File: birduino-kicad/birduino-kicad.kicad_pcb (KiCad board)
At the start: 2 copper layers, 47.5 x 71.9 mm, 38 parts, among them J1 Conn_01x03_Male, J10 Conn_01x02_Male, J11 Conn_01x01_Male, J2 Conn_01x02_Male, J3 Conn_02x05_Odd_Even, J4 Conn_01x04, J5 Conn_01x01_Male, J6 Conn_01x01_Male, J7 Conn_01x01_Male, J8 Conn_02x02_Odd_Even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

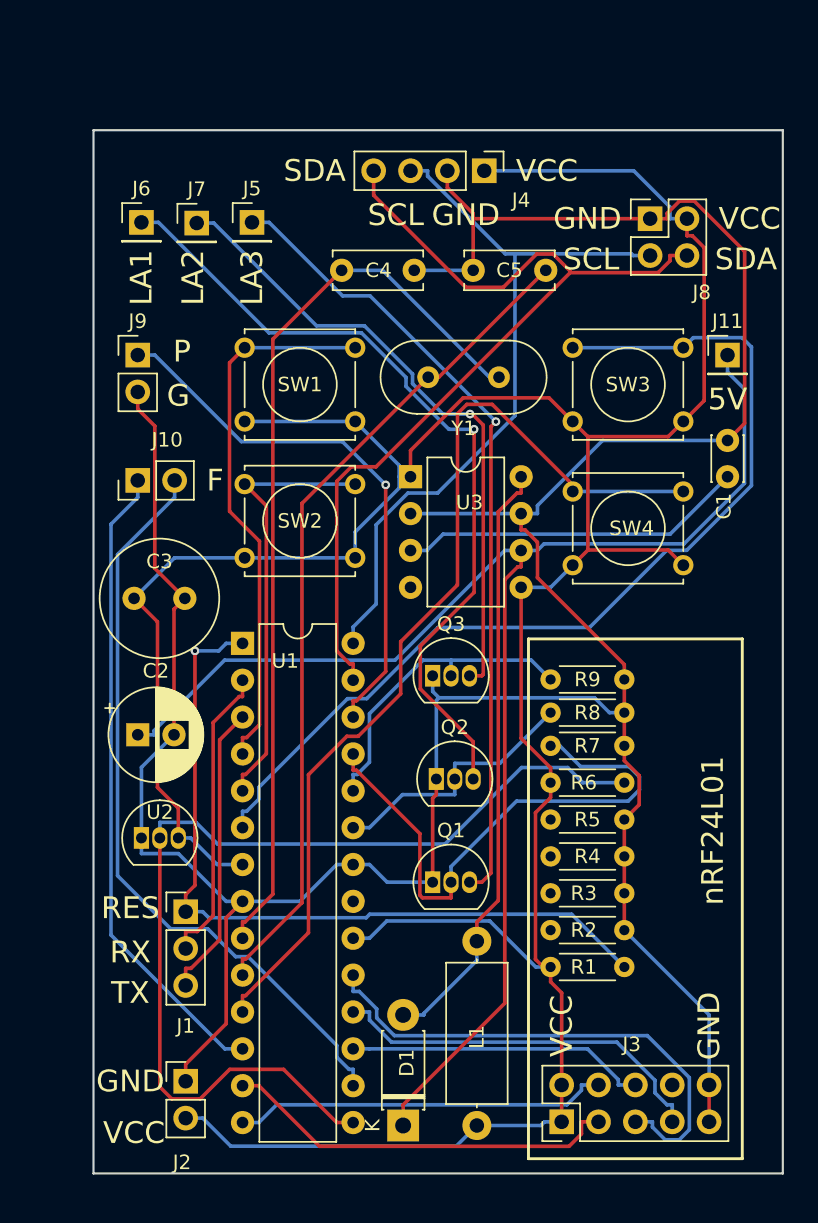
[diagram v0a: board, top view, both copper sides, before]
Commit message: feat: add fixation holes. First fabrication files. Version 1.0 closed for production.
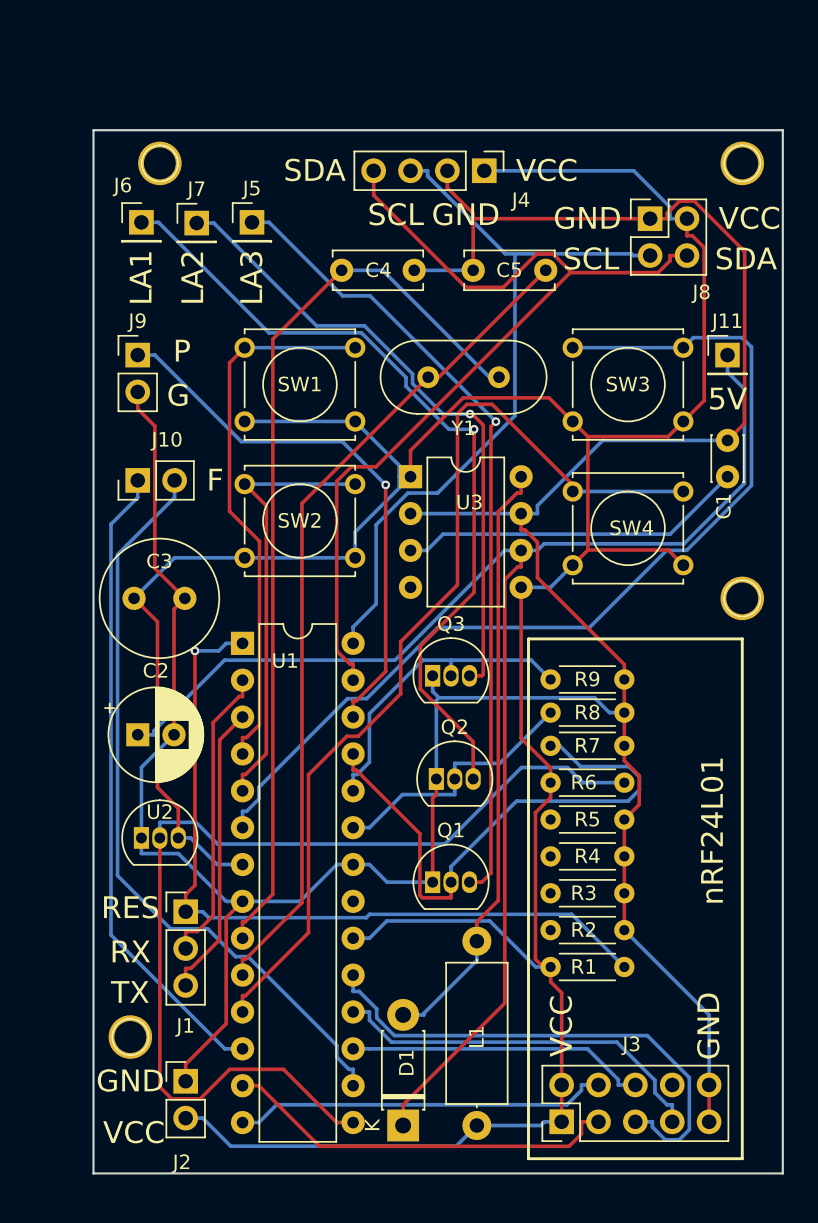
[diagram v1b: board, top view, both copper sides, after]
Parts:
- added ?: Pin_D1.0mm_L10.0mm, Connector_Pin:Pin_D1.0mm_L10.0mm, F.Cu at (133.3, 81.5)
- added ?: Pin_D1.0mm_L10.0mm, Connector_Pin:Pin_D1.0mm_L10.0mm, F.Cu at (173.5, 111.5)
- added ?: Pin_D1.0mm_L10.0mm, Connector_Pin:Pin_D1.0mm_L10.0mm, F.Cu at (173.5, 81.5)
- added ?: Pin_D1.0mm_L10.0mm, Connector_Pin:Pin_D1.0mm_L10.0mm, F.Cu at (131.3, 141.7)
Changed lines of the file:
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@@
     (tracks 429)
     (zones 0)
-    (modules 38)
+    (modules 42)
     (nets 32)
   )
@@
     (mod_text_size 1 1)
     (mod_text_width 0.15)
-    (pad_size 1.524 1.524)
-    (pad_drill 0.762)
+    (pad_size 3 3)
+    (pad_drill 2.2)
     (pad_to_mask_clearance 0.2)
     (solder_mask_min_width 0.25)
@@
     (visible_elements FFFFFF7F)
     (pcbplotparams
-      (layerselection 0x00030_80000001)
+      (layerselection 0x00030_ffffffff)
       (usegerberextensions false)
       (usegerberattributes false)
@@
       (outputformat 1)
       (mirror false)
-      (drillshape 1)
+      (drillshape 0)
       (scaleselection 1)
-      (outputdirectory ""))
+      (outputdirectory "../fabrication"))
   )
   (net 0 "")
@@
     (add_net XTAL2)
   )
+  (module Connector_Pin:Pin_D1.0mm_L10.0mm (layer F.Cu)
+    (at 133.35 81.534)
+    (descr "solder Pin_ diameter 1.0mm, hole diameter 1.0mm (press fit), length 10.0mm")
+    (tags "solder Pin_ press fit")
+    (fp_text reference "" (at -4.064 -0.508) (layer F.SilkS) hide
+      (effects (font (size 1 1) (thickness 0.15)))
+    )
+    (fp_text value Pin_D1.0mm_L10.0mm (at 0 -2.05) (layer F.Fab)
+      (effects (font (size 1 1) (thickness 0.15)))
+    )
+    (fp_text user %R (at 0 2.25) (layer F.Fab)
+      (effects (font (size 1 1) (thickness 0.15)))
+    )
+    (fp_circle (center 0 0) (end 1.5 0) (layer F.CrtYd) (width 0.05))
+    (fp_circle (center 0 0) (end 0.5 0) (layer F.Fab) (width 0.12))
+    (fp_circle (center 0 0) (end 1 0) (layer F.Fab) (width 0.12))
+    (fp_circle (center 0 0) (end 1.25 0.05) (layer F.SilkS) (width 0.12))
+    (pad 1 thru_hole circle (at 0 0) (size 3 3) (drill 2.2) (layers *.Cu *.Mask))
+    (model ${KISYS3DMOD}/Connector_Pin.3dshapes/Pin_D1.0mm_L10.0mm.wrl
+      (at (xyz 0 0 0))
+      (scale (xyz 1 1 1))
+      (rotate (xyz 0 0 0))
+    )
+  )
+  (module Connector_Pin:Pin_D1.0mm_L10.0mm (layer F.Cu)
+    (at 173.482 111.506)
+    (descr "solder Pin_ diameter 1.0mm, hole diameter 1.0mm (press fit), length 10.0mm")
+    (tags "solder Pin_ press fit")
+    (fp_text reference "" (at -4.064 -0.508) (layer F.SilkS) hide
+      (effects (font (size 1 1) (thickness 0.15)))
+    )
+    (fp_text value Pin_D1.0mm_L10.0mm (at 0 -2.05) (layer F.Fab)
+      (effects (font (size 1 1) (thickness 0.15)))
+    )
+    (fp_circle (center 0 0) (end 1.25 0.05) (layer F.SilkS) (width 0.12))
+    (fp_circle (center 0 0) (end 1 0) (layer F.Fab) (width 0.12))
+    (fp_circle (center 0 0) (end 0.5 0) (layer F.Fab) (width 0.12))
+    (fp_circle (center 0 0) (end 1.5 0) (layer F.CrtYd) (width 0.05))
+    (fp_text user %R (at 0 2.25) (layer F.Fab)
+      (effects (font (size 1 1) (thickness 0.15)))
+    )
+    (pad 1 thru_hole circle (at 0 0) (size 3 3) (drill 2.2) (layers *.Cu *.Mask))
+    (model ${KISYS3DMOD}/Connector_Pin.3dshapes/Pin_D1.0mm_L10.0mm.wrl
+      (at (xyz 0 0 0))
+      (scale (xyz 1 1 1))
+      (rotate (xyz 0 0 0))
+    )
+  )
+  (module Connector_Pin:Pin_D1.0mm_L10.0mm (layer F.Cu)
+    (at 173.482 81.534)
+    (descr "solder Pin_ diameter 1.0mm, hole diameter 1.0mm (press fit), length 10.0mm")
+    (tags "solder Pin_ press fit")
+    (fp_text reference "" (at -4.064 -0.508) (layer F.SilkS) hide
+      (effects (font (size 1 1) (thickness 0.15)))
+    )
+    (fp_text value Pin_D1.0mm_L10.0mm (at 0 -2.05) (layer F.Fab)
+      (effects (font (size 1 1) (thickness 0.15)))
+    )
+    (fp_text user %R (at 0 2.25) (layer F.Fab)
+      (effects (font (size 1 1) (thickness 0.15)))
+    )
+    (fp_circle (center 0 0) (end 1.5 0) (layer F.CrtYd) (width 0.05))
+    (fp_circle (center 0 0) (end 0.5 0) (layer F.Fab) (width 0.12))
+    (fp_circle (center 0 0) (end 1 0) (layer F.Fab) (width 0.12))
+    (fp_circle (center 0 0) (end 1.25 0.05) (layer F.SilkS) (width 0.12))
+    (pad 1 thru_hole circle (at 0 0) (size 3 3) (drill 2.2) (layers *.Cu *.Mask))
+    (model ${KISYS3DMOD}/Connector_Pin.3dshapes/Pin_D1.0mm_L10.0mm.wrl
+      (at (xyz 0 0 0))
+      (scale (xyz 1 1 1))
+      (rotate (xyz 0 0 0))
+    )
+  )
+  (module Connector_Pin:Pin_D1.0mm_L10.0mm (layer F.Cu)
+    (at 131.318 141.732)
+    (descr "solder Pin_ diameter 1.0mm, hole diameter 1.0mm (press fit), length 10.0mm")
+    (tags "solder Pin_ press fit")
+    (fp_text reference "" (at -4.064 -0.508) (layer F.SilkS) hide
+      (effects (font (size 1 1) (thickness 0.15)))
+    )
+    (fp_text value Pin_D1.0mm_L10.0mm (at 0 -2.05) (layer F.Fab)
+      (effects (font (size 1 1) (thickness 0.15)))
+    )
+    (fp_circle (center 0 0) (end 1.25 0.05) (layer F.SilkS) (width 0.12))
+    (fp_circle (center 0 0) (end 1 0) (layer F.Fab) (width 0.12))
+    (fp_circle (center 0 0) (end 0.5 0) (layer F.Fab) (width 0.12))
+    (fp_circle (center 0 0) (end 1.5 0) (layer F.CrtYd) (width 0.05))
+    (fp_text user %R (at 0 2.25) (layer F.Fab)
+      (effects (font (size 1 1) (thickness 0.15)))
+    )
+    (pad 1 thru_hole circle (at 0 0) (size 3 3) (drill 2.2) (layers *.Cu *.Mask))
+    (model ${KISYS3DMOD}/Connector_Pin.3dshapes/Pin_D1.0mm_L10.0mm.wrl
+      (at (xyz 0 0 0))
+      (scale (xyz 1 1 1))
+      (rotate (xyz 0 0 0))
+    )
+  )
   (module Connector_PinHeader_2.54mm:PinHeader_1x03_P2.54mm_Vertical (layer F.Cu)
     (at 135.128 133.096)
@@
     (descr "Through hole straight pin header, 1x01, 2.54mm pitch, single row")
     (tags "Through hole pin header THT 1x01 2.54mm single row")
-    (fp_text reference J6 (at 0 -2.33) (layer F.SilkS)
-      (effects (font (size 1 1) (thickness 0.15)))
-    )
+    (fp_text reference J6 (at -1.27 -2.54) (layer F.SilkS)
+      (effects (font (size 1 1) (thickness 0.15)))
+    )

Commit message: feat: Version 1.1. Better size, ground plat and proper fabrication files.
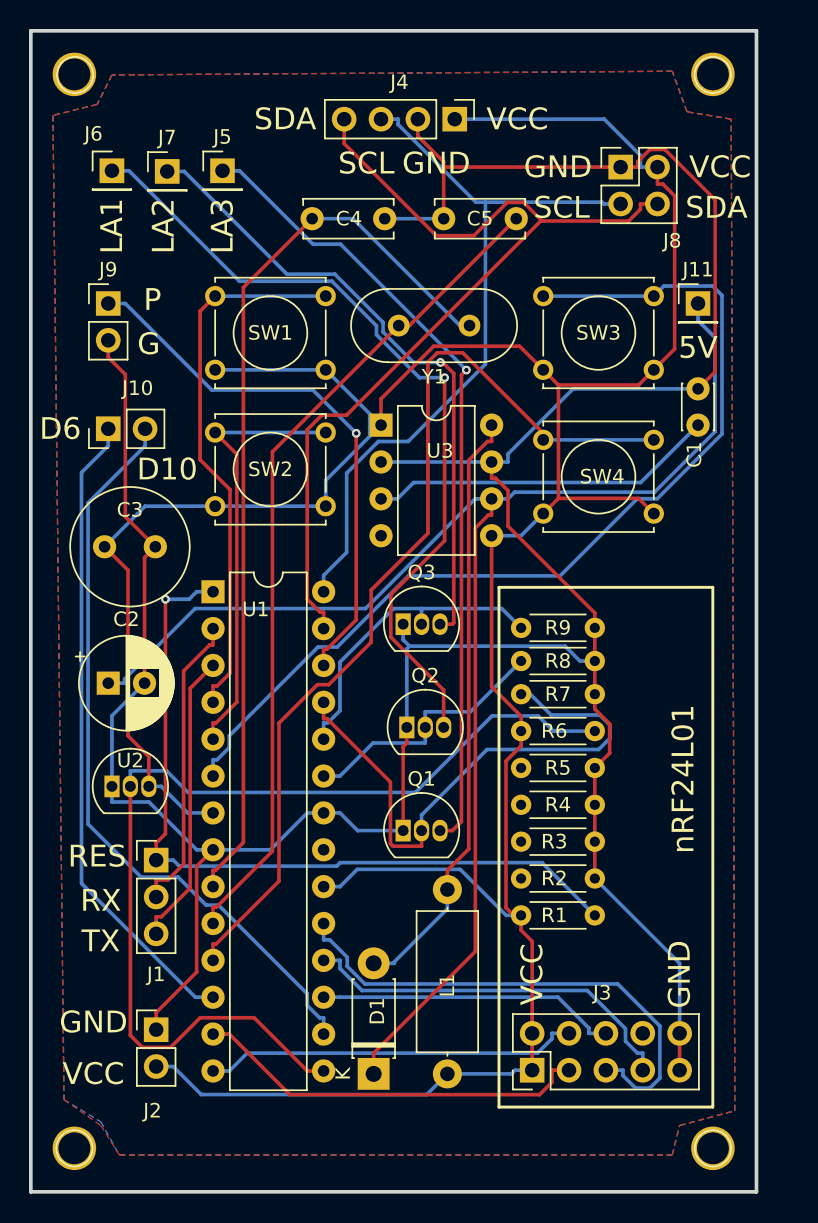
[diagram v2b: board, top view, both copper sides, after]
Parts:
- moved ? 59.6 mm to (127.5, 149.4)
- moved ? 40.9 mm to (171.5, 149.4)
- moved ? 8.44 mm to (127.5, 75.4)
- moved ? 6.43 mm to (171.4, 75.4)
- moved C4 4.10 mm to (143.8, 85.3)
- moved C5 4.10 mm to (152.9, 85.3)
- moved D1 4.10 mm to (148.1, 144.3)
- moved J3 4.10 mm to (159.0, 144.0)
- moved R1 4.10 mm to (163.3, 133.3)
- moved R2 4.10 mm to (163.3, 130.8)
- moved SW2 4.10 mm to (137.2, 100.1)
- moved C1 4.10 mm to (170.4, 99.6)
- moved C3 4.10 mm to (129.5, 108.0)
- moved J11 4.10 mm to (170.4, 91.2)
- moved J4 4.10 mm to (153.7, 78.5)
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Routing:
- added copper zone on B.Cu, net GND
- added copper zone on F.Cu, net GND
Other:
- board size 47.5 x 71.9 mm -> 50 x 80 mm
- board text added: "D10"
- board text added: "D6"
- board text added: "birduino 1.1 2019 (c) Designed in Berlin"
- board text removed: "F"
- board text removed: "birduino 1.0 2019 (c) Designed in Berlin"
